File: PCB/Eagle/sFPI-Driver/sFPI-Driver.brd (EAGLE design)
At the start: 100 x 80 mm, 31 parts, among them IC1 ATMEGA168-PU, U1 LT1006CN8PBF, U2 LT1006CN8PBF, U3 LT1006CN8PBF, U4 LT1006CN8PBF, U5 LT1006CN8PBF, U6 LT1006CN8PBF

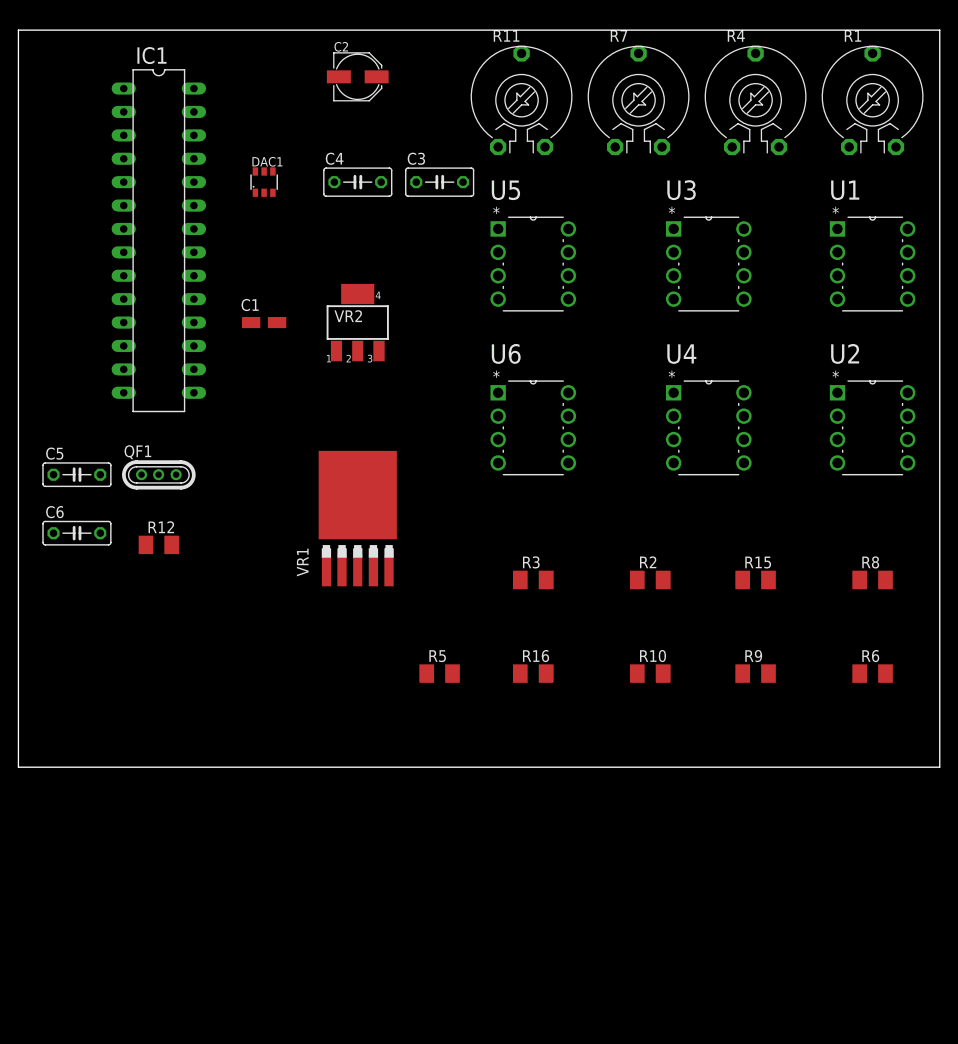
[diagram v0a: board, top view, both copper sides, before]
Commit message: sFPI - Updated Parts List - Updated LTSpice Models and Scripts
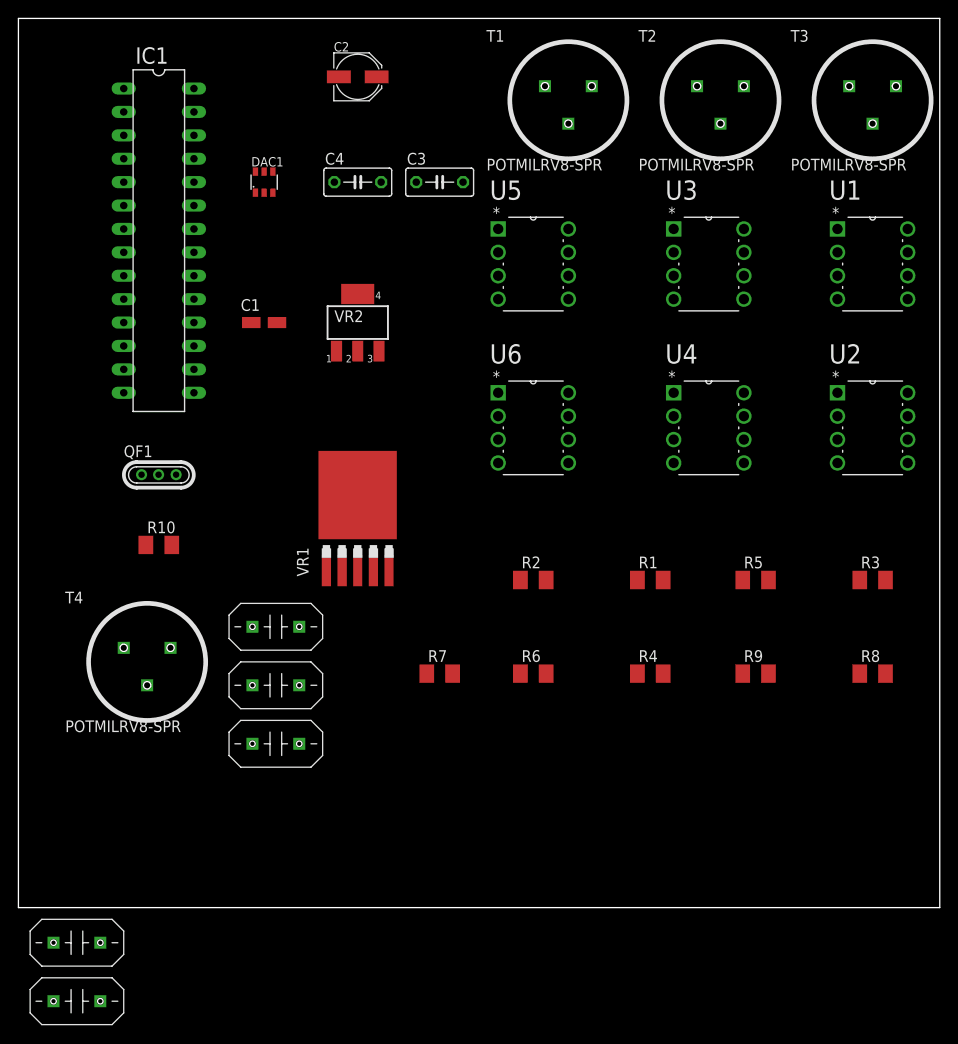
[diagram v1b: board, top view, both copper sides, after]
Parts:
- removed R11: (no value), rcl:PT-10
- removed R12, R16: 10k, rcl:M1206
- removed R15: 3.3k, rcl:M1206
- added C7, C8, C9: CAP-CER-22PF-50V-NP0-RADIAL, sFPI:FG28
- added T1, T2, T3, T4: POTMILRV8-SPR, sFPI:SPR
- C5, C6: value (none) -> CAP-CER-22PF-50V-NP0-RADIAL; device rcl:C050-025X075 -> sFPI:FG28
- R1, R4: value (none) -> 10k; device rcl:PT-10 -> rcl:M1206
- R3, R5: value 10k -> 3.3k
- R7: value (none) -> 1M; device rcl:PT-10 -> rcl:M1206
- R8: value 3.3k -> 1M
- R9: value 10k -> 1M
- moved R7 65.9 mm to (45.7, 10.2)
- moved R4 63.3 mm to (68.6, 10.2)
- moved R1 57.4 mm to (68.6, 20.3)
- moved R10 55.1 mm to (15.2, 24.1)
- moved C5 50.8 mm to (6.35, -19.1)
- moved C6 50.8 mm to (6.35, -25.4)
- moved R3 36.8 mm to (92.7, 20.3)
- moved R6 36.8 mm to (55.9, 10.2)
- moved R5 35.8 mm to (80.0, 20.3)
- moved R2 12.7 mm to (55.9, 20.3)
- moved R8 10.2 mm to (92.7, 10.2)
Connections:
- new net N$13: R5.2, T3.2
- net GND: now also C5.P$1, C6.P$1, C7.P$1, C8.P$1, C9.P$1; no longer C5.2, C6.2
- net N$1: now also C5.P$2; no longer C5.1
- net N$10: now also R1.2, T1.2; no longer C2.+, R11.3
- net N$12: now also R3.2, T2.2; no longer R1.2, R15.2, R7.2, R8.2
- net N$14: now also C9.P$2, R5.1, R6.2; no longer R15.1, R16.2
- net N$16: now also R6.1; no longer R16.1
- net N$17: now also R8.2; no longer R6.2
- net N$19: now also R7.1, R8.1; no longer R5.1, R6.1
- net N$2: now also C6.P$2; no longer C6.1
- net N$23: now also T4.2; no longer R4.2
- net N$24: now also R7.2; no longer R5.2
- net N$3: now also R10.1; no longer R12.1
- net N$4: now also R10.2; no longer R12.2
- net N$5: now also R2.1, T2.3, T3.3; no longer R1.3, R3.1, R7.3
- net N$6: now also C7.P$2, C8.P$2, R1.1, R2.2, R3.1, R4.2; no longer R10.2, R2.1, R3.2, R8.1
- net N$9: now also C2.+, T1.3; no longer R11.2, R2.2
- net V-: now also T4.3; no longer R4.3
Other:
- board size 100 x 80 mm -> 100 x 96.5 mm
